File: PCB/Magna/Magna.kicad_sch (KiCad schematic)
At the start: 8 parts

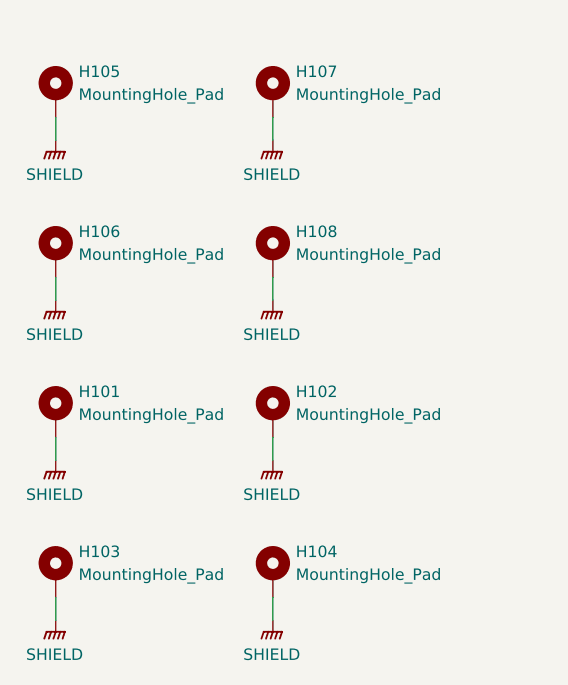
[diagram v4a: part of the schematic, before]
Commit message: Update Project to Kicad 8.0 and prepare for production
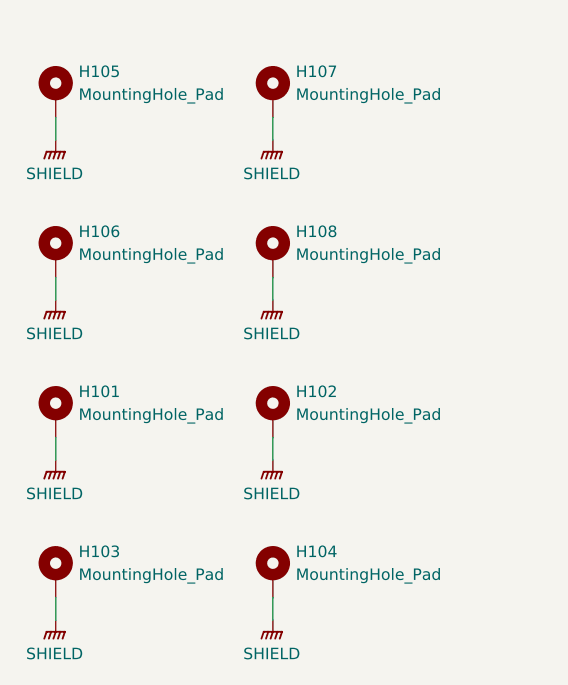
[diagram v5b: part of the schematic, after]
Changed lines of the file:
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@@
 	)
 	(symbol
-		(lib_id "Skrooter_symbols:SHIELD")
+		(lib_id "SkrooterLib:SHIELD")
 		(at 52.07 161.29 0)
 		(unit 1)
@@
 		)
 		(property "Value" "SHIELD"
-			(at 51.943 165.1 0)
+			(at 51.943 165.0167 0)
 			(effects
 				(font
@@
 			)
 		)
-		(property "Description" ""
+		(property "Description" "Power symbol creates a global label with name \"GNDPWR\" , power ground"
 			(at 52.07 161.29 0)
 			(effects
@@
 			)
 		)
-		(property "Description" ""
+		(property "Description" "Mounting Hole with connection"
 			(at 27.94 138.43 0)
 			(effects
@@
 			)
 		)
+		(property "LSCS" ""
+			(at 27.94 138.43 0)
+			(effects
+				(font
+					(size 1.27 1.27)
+				)
+				(hide yes)
+			)
+		)
 		(pin "1"
 		)
@@
 	)
 	(symbol
-		(lib_id "Skrooter_symbols:SHIELD")
+		(lib_id "SkrooterLib:SHIELD")
 		(at 52.07 107.95 0)
 		(unit 1)
@@
 		)
 		(property "Value" "SHIELD"
-			(at 51.943 111.76 0)
+			(at 51.943 111.6767 0)
 			(effects
 				(font
@@
 			)
 		)
-		(property "Description" ""
+		(property "Description" "Power symbol creates a global label with name \"GNDPWR\" , power ground"
 			(at 52.07 107.95 0)
 			(effects
@@
 			)
 		)
-		(property "Description" ""
+		(property "Description" "Mounting Hole with connection"
+			(at 52.07 156.21 0)
+			(effects
+				(font
+					(size 1.27 1.27)
+				)
+				(hide yes)
+			)
+		)
+		(property "LSCS" ""
 			(at 52.07 156.21 0)
 			(effects
@@
 			)
 		)
-		(property "Description" ""
+		(property "Description" "Mounting Hole with connection"
 			(at 27.94 156.21 0)
 			(effects
@@
 			)
 		)
+		(property "LSCS" ""
+			(at 27.94 156.21 0)
+			(effects
+				(font
+					(size 1.27 1.27)
+				)
+				(hide yes)
+			)
+		)
 		(pin "1"
 		)
@@
 	)
 	(symbol
-		(lib_id "Skrooter_symbols:SHIELD")
+		(lib_id "SkrooterLib:SHIELD")
 		(at 27.94 125.73 0)
 		(unit 1)
@@
 		)
 		(property "Value" "SHIELD"
-			(at 27.813 129.54 0)
+			(at 27.813 129.4567 0)
 			(effects
 				(font
@@
 			)
 		)
-		(property "Description" ""
+		(property "Description" "Power symbol creates a global label with name \"GNDPWR\" , power ground"
 			(at 27.94 125.73 0)
 			(effects
@@
 	)
 	(symbol
-		(lib_id "Skrooter_symbols:SHIELD")
+		(lib_id "SkrooterLib:SHIELD")
 		(at 52.07 125.73 0)
 		(unit 1)
@@
 		)
 		(property "Value" "SHIELD"
-			(at 51.943 129.54 0)
+			(at 51.943 129.4567 0)
 			(effects
 				(font
@@
 			)
 		)
-		(property "Description" ""
+		(property "Description" "Power symbol creates a global label with name \"GNDPWR\" , power ground"
 			(at 52.07 125.73 0)
 			(effects
@@
 	)
 	(symbol
-		(lib_id "Skrooter_symbols:SHIELD")
+		(lib_id "SkrooterLib:SHIELD")
 		(at 27.94 143.51 0)
 		(unit 1)
@@
 		)
 		(property "Value" "SHIELD"
-			(at 27.813 147.32 0)
+			(at 27.813 147.2367 0)
 			(effects
 				(font
@@
 			)
 		)
-		(property "Description" ""
+		(property "Description" "Power symbol creates a global label with name \"GNDPWR\" , power ground"
 			(at 27.94 143.51 0)
 			(effects
@@
 			)
 		)
-		(property "Description" ""
+		(property "Description" "Mounting Hole with connection"
 			(at 27.94 102.87 0)
 			(effects
@@
 			)
 		)
+		(property "LSCS" ""
+			(at 27.94 102.87 0)
+			(effects
+				(font
+					(size 1.27 1.27)
+				)
+				(hide yes)
+			)
+		)
 		(pin "1"
 		)
@@
 	)
 	(symbol
-		(lib_id "Skrooter_symbols:SHIELD")
+		(lib_id "SkrooterLib:SHIELD")
 		(at 27.94 161.29 0)
 		(unit 1)
@@
 		)
 		(property "Value" "SHIELD"
-			(at 27.813 165.1 0)
+			(at 27.813 165.0167 0)
 			(effects
 				(font
@@
 			)
 		)
-		(property "Description" ""
+		(property "Description" "Power symbol creates a global label with name \"GNDPWR\" , power ground"
 			(at 27.94 161.29 0)
 			(effects
@@
 			)
 		)
-		(property "Description" ""
+		(property "Description" "Mounting Hole with connection"
+			(at 52.07 138.43 0)
+			(effects
+				(font
+					(size 1.27 1.27)
+				)
+				(hide yes)
+			)
+		)
+		(property "LSCS" ""
 			(at 52.07 138.43 0)
 			(effects
@@
 			)
 		)
-		(property "Description" ""
+		(property "Description" "Mounting Hole with connection"
+			(at 27.94 120.65 0)
+			(effects
+				(font
+					(size 1.27 1.27)
+				)
+				(hide yes)
+			)
+		)
+		(property "LSCS" ""
 			(at 27.94 120.65 0)
 			(effects
@@
 			)
 		)
-		(property "Description" ""
+		(property "Description" "Mounting Hole with connection"
 			(at 52.07 102.87 0)
 			(effects
@@
 			)
 		)
+		(property "LSCS" ""
+			(at 52.07 102.87 0)
+			(effects
+				(font
+					(size 1.27 1.27)
+				)
+				(hide yes)
+			)
+		)
 		(pin "1"
 		)
@@
 	)
 	(symbol
-		(lib_id "Skrooter_symbols:SHIELD")
+		(lib_id "SkrooterLib:SHIELD")
 		(at 52.07 143.51 0)
 		(unit 1)
@@
 		)
 		(property "Value" "SHIELD"
-			(at 51.943 147.32 0)
+			(at 51.943 147.2367 0)
 			(effects
 				(font
@@
 			)
 		)
-		(property "Description" ""
+		(property "Description" "Power symbol creates a global label with name \"GNDPWR\" , power ground"
 			(at 52.07 143.51 0)
 			(effects
@@
 	)
 	(symbol
-		(lib_id "Skrooter_symbols:SHIELD")
+		(lib_id "SkrooterLib:SHIELD")
 		(at 27.94 107.95 0)
 		(unit 1)
@@
 		)
 		(property "Value" "SHIELD"
-			(at 27.813 111.76 0)
+			(at 27.813 111.6767 0)
 			(effects
 				(font
@@
 			)
 		)
-		(property "Description" ""
+		(property "Description" "Power symbol creates a global label with name \"GNDPWR\" , power ground"
 			(at 27.94 107.95 0)
 			(effects
@@
 			)
 		)
-		(property "Description" ""
+		(property "Description" "Mounting Hole with connection"
 			(at 52.07 120.65 0)
 			(effects
+				(font
+					(size 1.27 1.27)
+				)
+				(hide yes)
+			)
+		)
+		(property "LSCS" ""
+			(at 52.07 120.65 0)
+			(effects

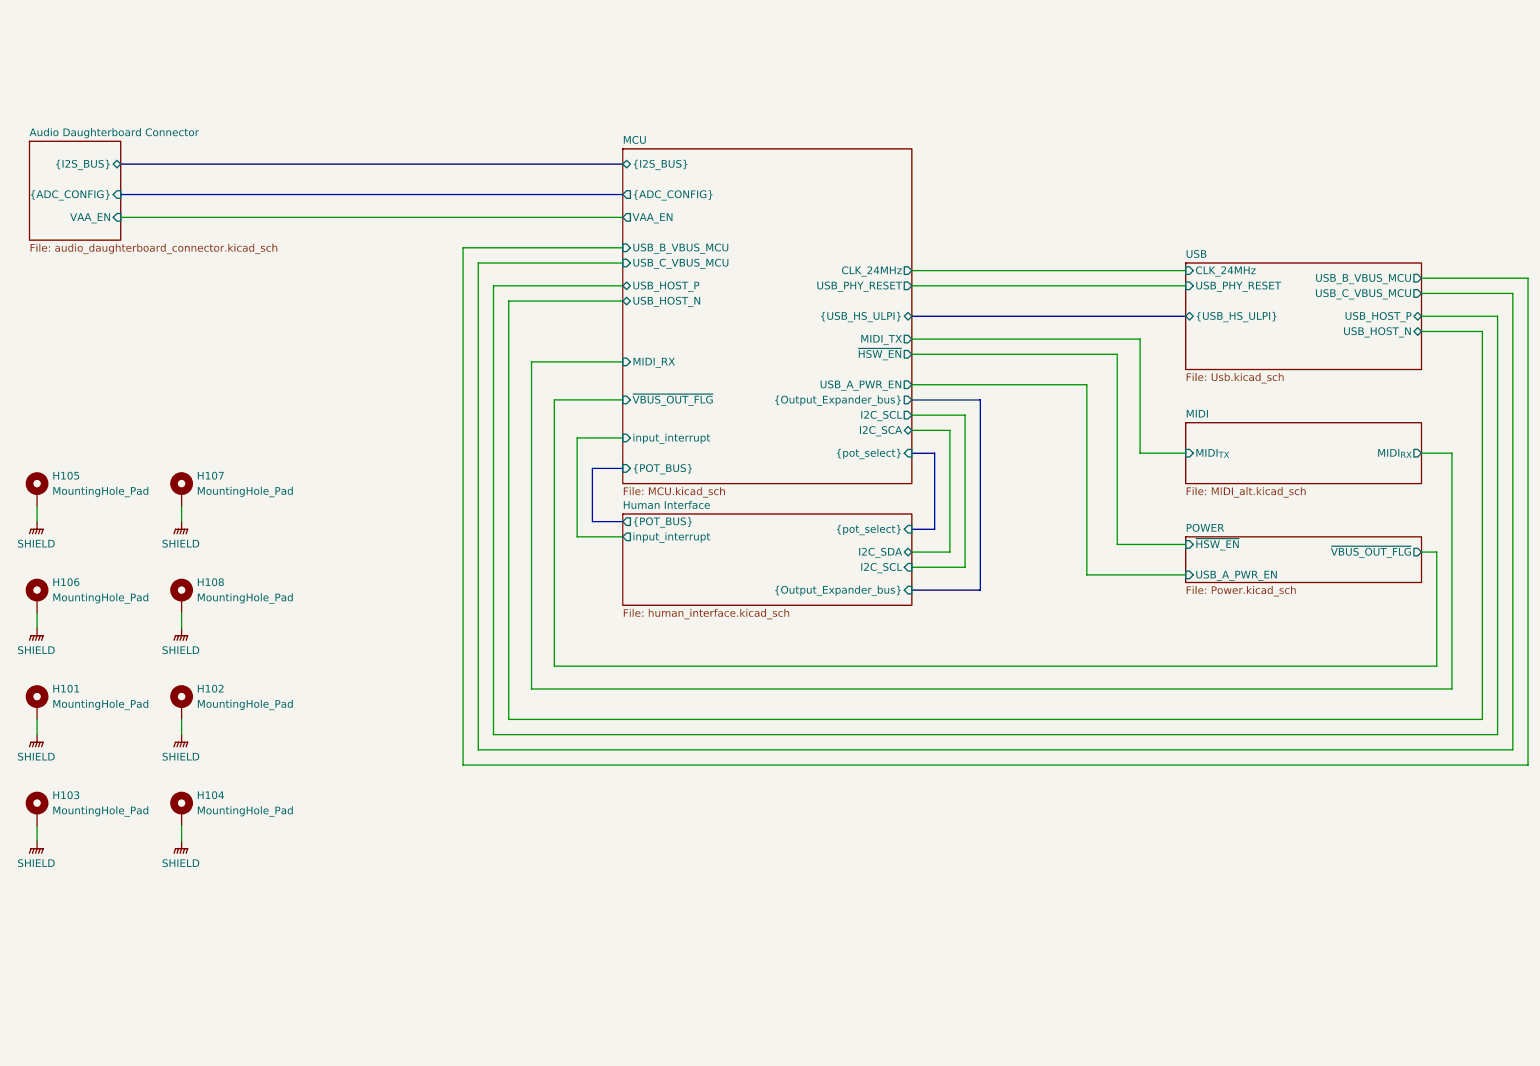
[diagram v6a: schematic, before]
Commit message: Update Mainboard PCB
* Added better power ORing
* Added DRC for length matching
* Changed out components for cheaper production
* Removed some optional circuits from BOM for first prototype
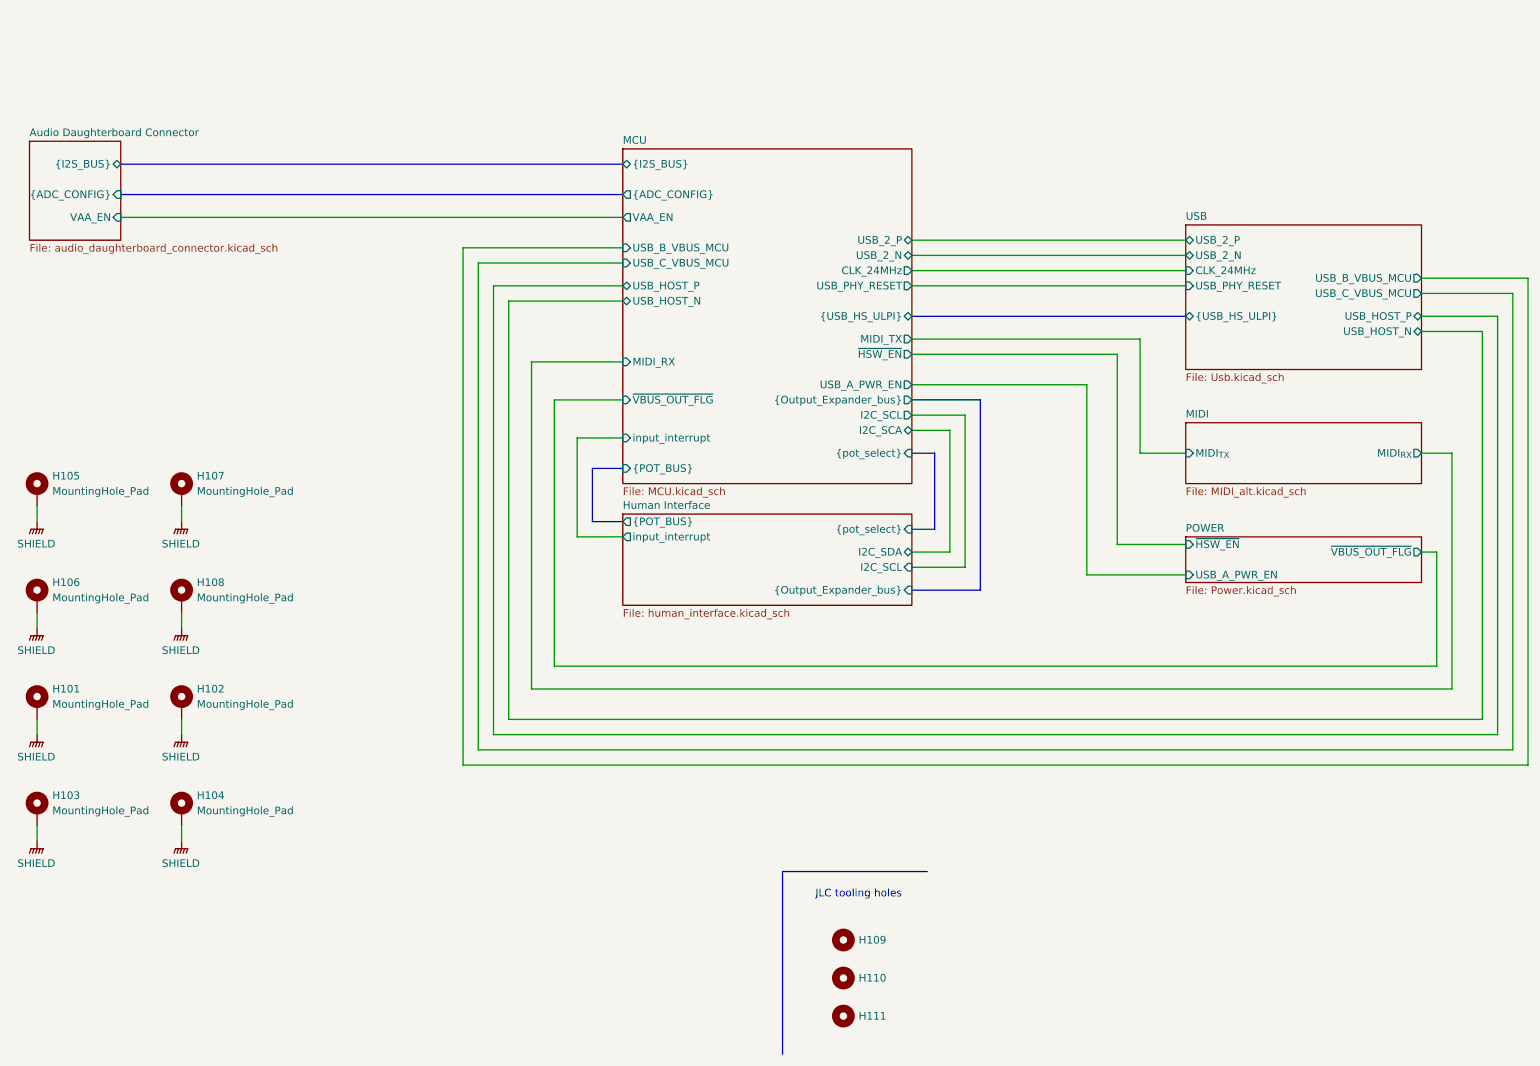
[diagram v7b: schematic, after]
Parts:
- added H109, H110, H111: MountingHole, MountingHole:ToolingHole_1.152mm, symbol Mechanical:MountingHole
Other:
- sheet MCU ports: added USB_2_N, USB_2_P; removed none
- sheet USB ports: added USB_2_N, USB_2_P; removed none
- note added: "JLC tooling holes"
